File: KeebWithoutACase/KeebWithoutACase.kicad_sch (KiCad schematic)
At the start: 104 parts, among them SW1 SW_Push_45deg, SW10 SW_Push_45deg, SW11 SW_Push_45deg, SW12 SW_Push_45deg, SW13 SW_Push_45deg, SW14 SW_Push_45deg, SW15 SW_Push_45deg, SW16 SW_Push_45deg, SW17 SW_Push_45deg, SW18 SW_Push_45deg, SW19 SW_Push_45deg, SW2 SW_Push_45deg, SW20 SW_Push_45deg, SW21 SW_Push_45deg, SW22 SW_Push_45deg, SW23 SW_Push_45deg, SW24 SW_Push_45deg, SW25 SW_Push_45deg, SW26 SW_Push_45deg, SW27 SW_Push_45deg, SW28 SW_Push_45deg, SW29 SW_Push_45deg, SW3 SW_Push_45deg, SW30 SW_Push_45deg, SW31 SW_Push_45deg, SW32 SW_Push_45deg, SW33 SW_Push_45deg, SW34 SW_Push_45deg, SW35 SW_Push_45deg, SW36 SW_Push_45deg, SW37 SW_Push_45deg, SW38 SW_Push_45deg, SW39 SW_Push_45deg, SW4 SW_Push_45deg, SW40 SW_Push_45deg, SW41 SW_Push_45deg, SW42 SW_Push_45deg, SW43 SW_Push_45deg, SW44 SW_Push_45deg, SW45 SW_Push_45deg, SW46 SW_Push_45deg, SW47 SW_Push_45deg, SW48 SW_Push_45deg, SW49 SW_Push_45deg, SW5 SW_Push_45deg, SW50 SW_Push_45deg, SW51 SW_Push_45deg, SW52 SW_Push_45deg, SW6 SW_Push_45deg, SW7 SW_Push_45deg, SW8 SW_Push_45deg, SW9 SW_Push_45deg

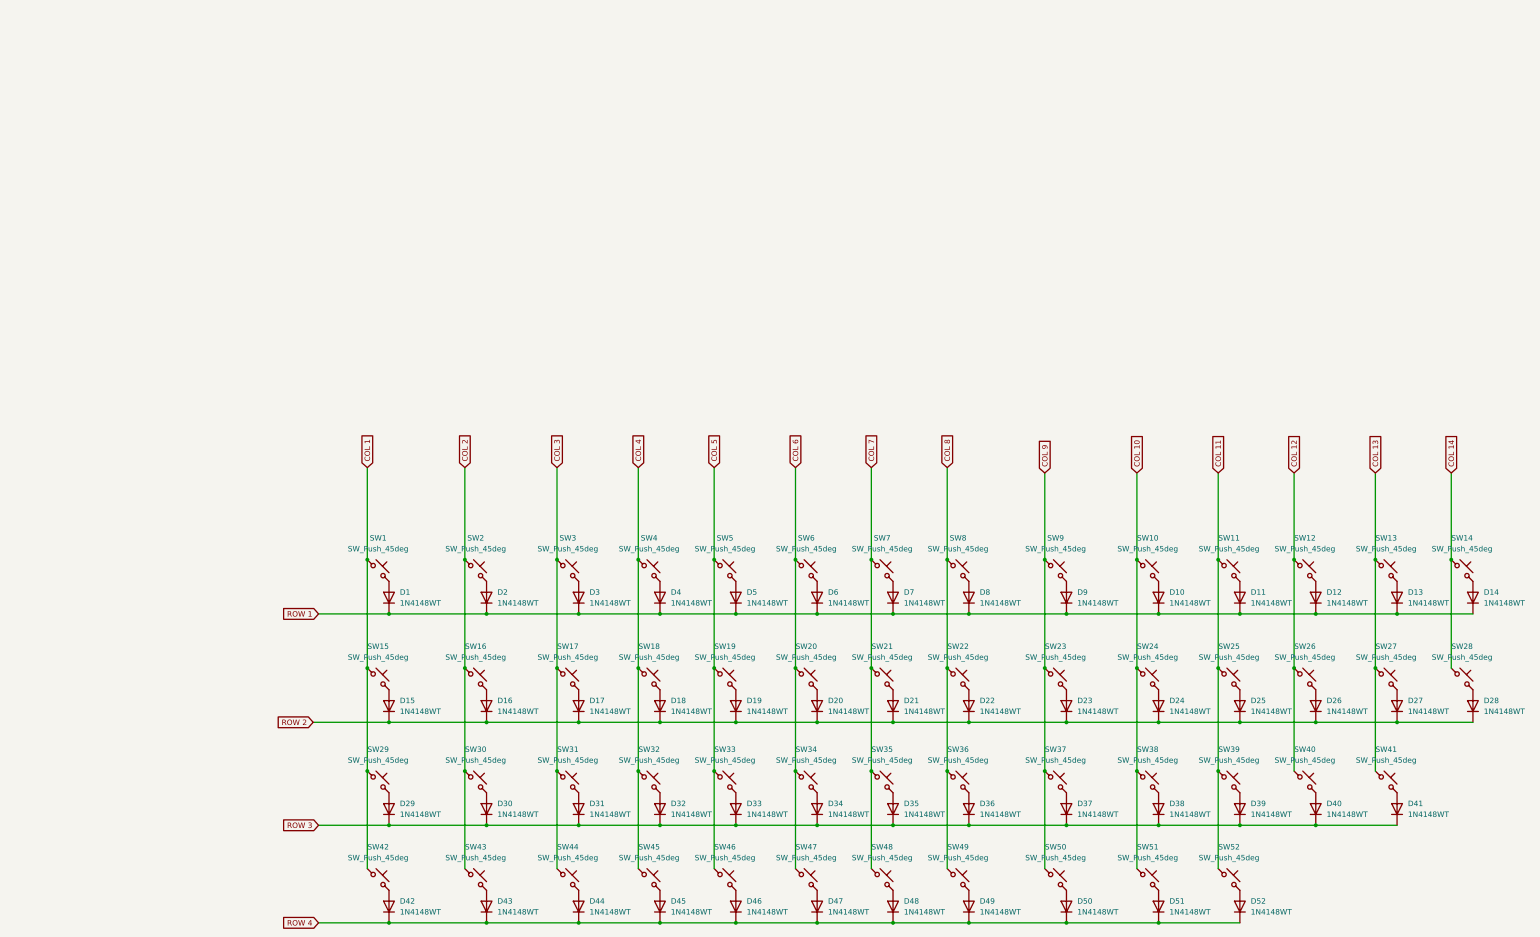
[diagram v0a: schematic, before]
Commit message: updated the schematic of the pcb to include the missing row
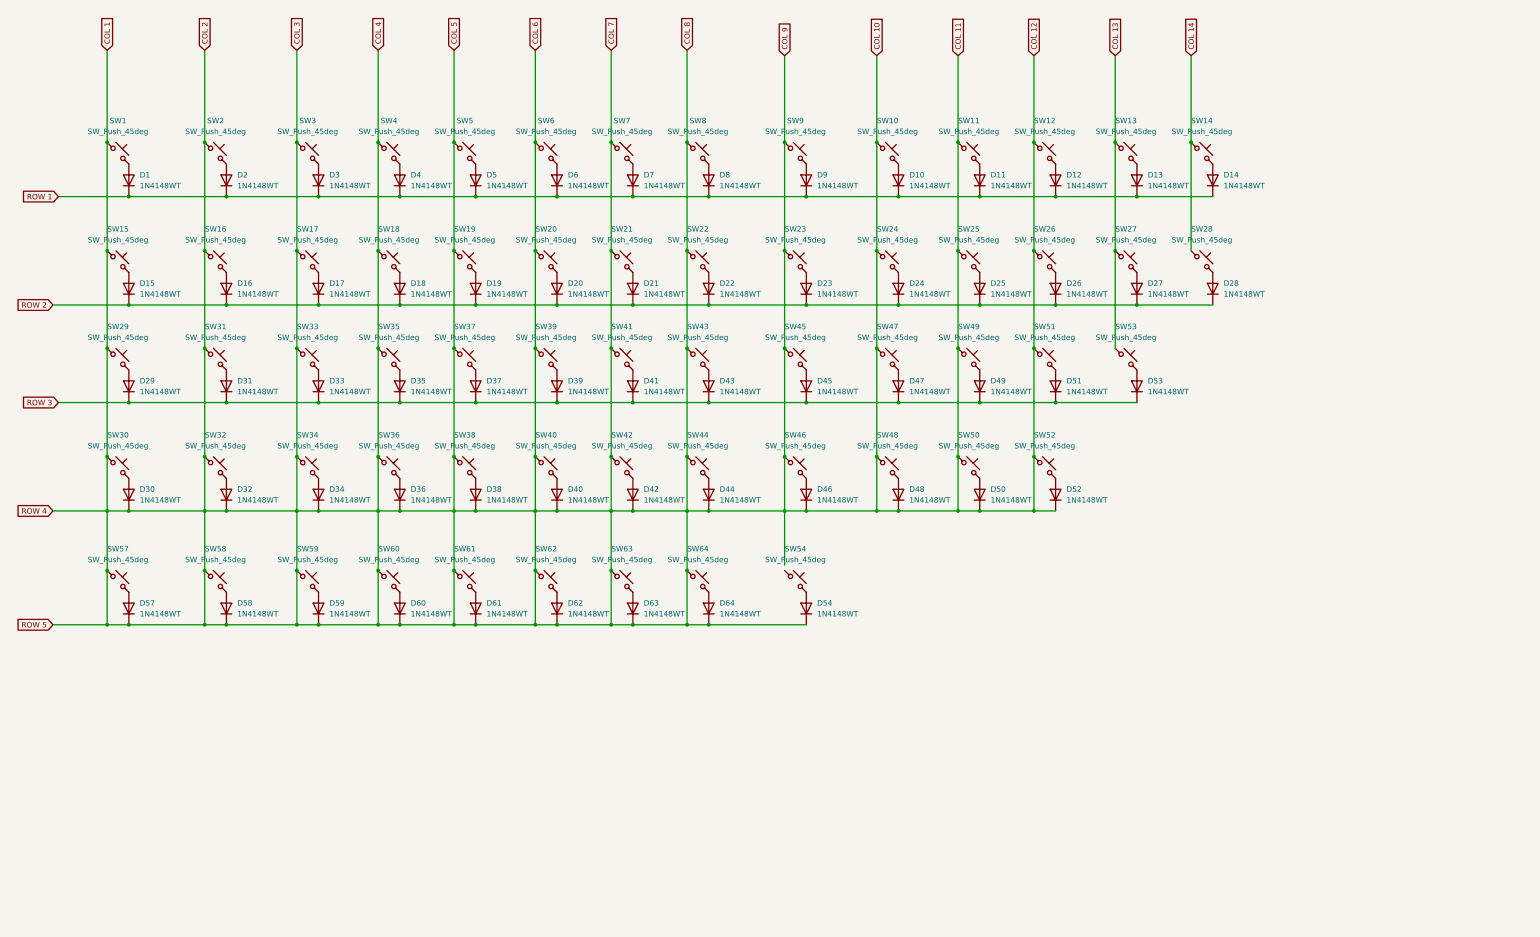
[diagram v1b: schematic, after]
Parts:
- added D53, D54, D57, D58, D59, D60, D61, D62, D63, D64: 1N4148WT, Diode_SMD:D_SOD-523, symbol Diode:1N4148WT
- added SW53, SW54, SW57, SW58, SW59, SW60, SW61, SW62, SW63, SW64: SW_Push_45deg, symbol Switch:SW_Push_45deg
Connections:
- net COL 10 is gone; now on net COL 1: SW10.1, SW24.1, SW38.1, SW51.1
- net COL 11 is gone; now on net COL 1: SW11.1, SW25.1, SW39.1, SW52.1
- net COL 12 is gone; now on net COL 1: SW12.1, SW26.1, SW40.1
- net COL 2 is gone; now on net COL 1: SW16.1, SW2.1, SW30.1, SW43.1
- net COL 3 is gone; now on net COL 1: SW17.1, SW3.1, SW31.1, SW44.1
- net COL 4 is gone; now on net COL 1: SW18.1, SW32.1, SW4.1, SW45.1
- net COL 5 is gone; now on net COL 1: SW19.1, SW33.1, SW46.1, SW5.1
- net COL 6 is gone; now on net COL 1: SW20.1, SW34.1, SW47.1, SW6.1
- net COL 7 is gone; now on net COL 1: SW21.1, SW35.1, SW48.1, SW7.1
- net COL 8 is gone; now on net COL 1: SW22.1, SW36.1, SW49.1, SW8.1
- net COL 9 is gone; now on net COL 1: SW23.1, SW37.1, SW50.1, SW9.1
- net COL 1: now also D30.1 (K), D32.1 (K), D34.1 (K), D36.1 (K), D38.1 (K), D40.1 (K), D42.1 (K), D44.1 (K), D46.1 (K), D48.1 (K), D50.1 (K), D52.1 (K), SW41.1, D54.1 (K), D57.1 (K), D58.1 (K), D59.1 (K), D60.1 (K), D61.1 (K), D62.1 (K), D63.1 (K), D64.1 (K), SW57.1, SW58.1, SW59.1, SW60.1, SW61.1, SW62.1, SW63.1, SW64.1
- net COL 13: now also SW53.1; no longer SW41.1
- net ROW 3: now also D43.1 (K), D45.1 (K), D47.1 (K), D49.1 (K), D51.1 (K), D53.1 (K); no longer D30.1 (K), D32.1 (K), D34.1 (K), D36.1 (K), D38.1 (K), D40.1 (K)
- removed net ROW 4: D42.1 (K), D43.1 (K), D44.1 (K), D45.1 (K), D46.1 (K), D47.1 (K), D48.1 (K), D49.1 (K), D50.1 (K), D51.1 (K), D52.1 (K)
- new net: D53.2 (A), SW53.2
- new net: D60.2 (A), SW60.2
- new net: D57.2 (A), SW57.2
- new net: D62.2 (A), SW62.2
- new net: D54.2 (A), SW54.2
- new net: D63.2 (A), SW63.2
- new net: D64.2 (A), SW64.2
- new net: D58.2 (A), SW58.2
- new net: D61.2 (A), SW61.2
- new net: D59.2 (A), SW59.2
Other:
- moved on the sheet: D1, D10, D11, D12, D13, D14, D15, D16, D17, D18, D19, D2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

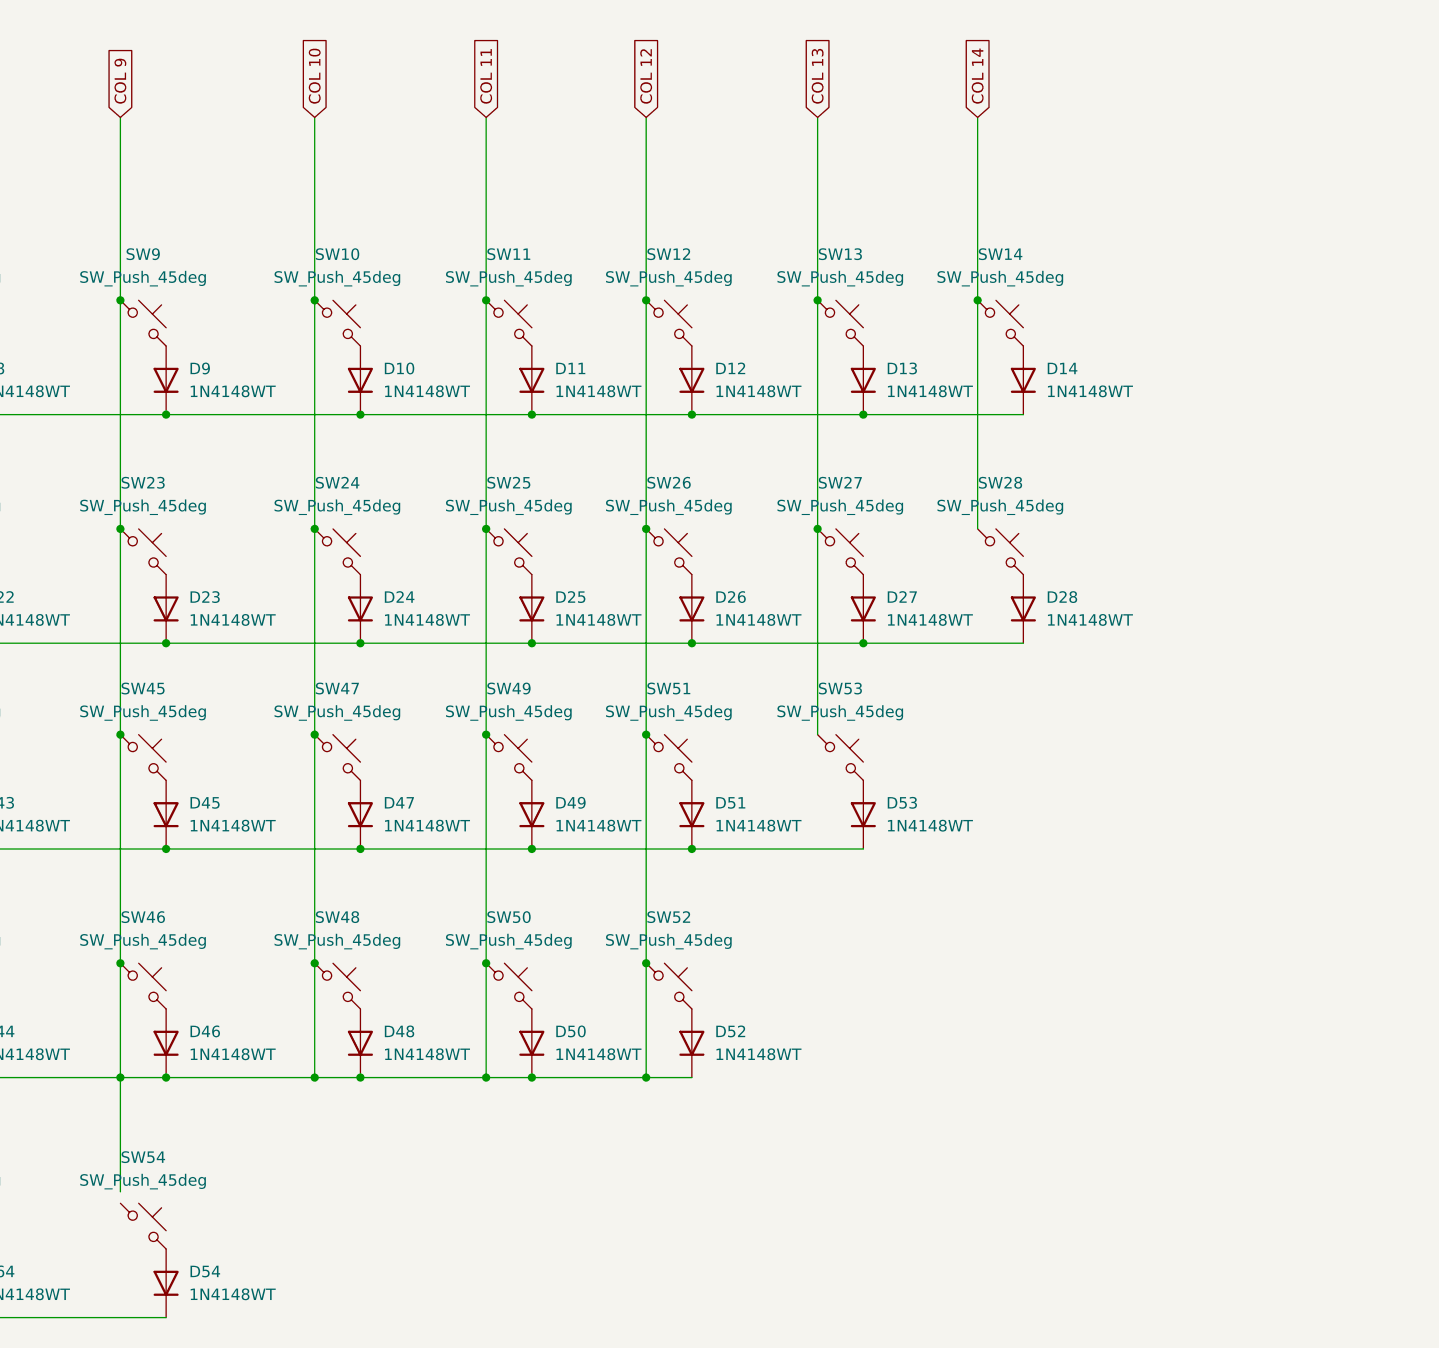
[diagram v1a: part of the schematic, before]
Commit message: updated the schem to incorporate those extra 4 keys
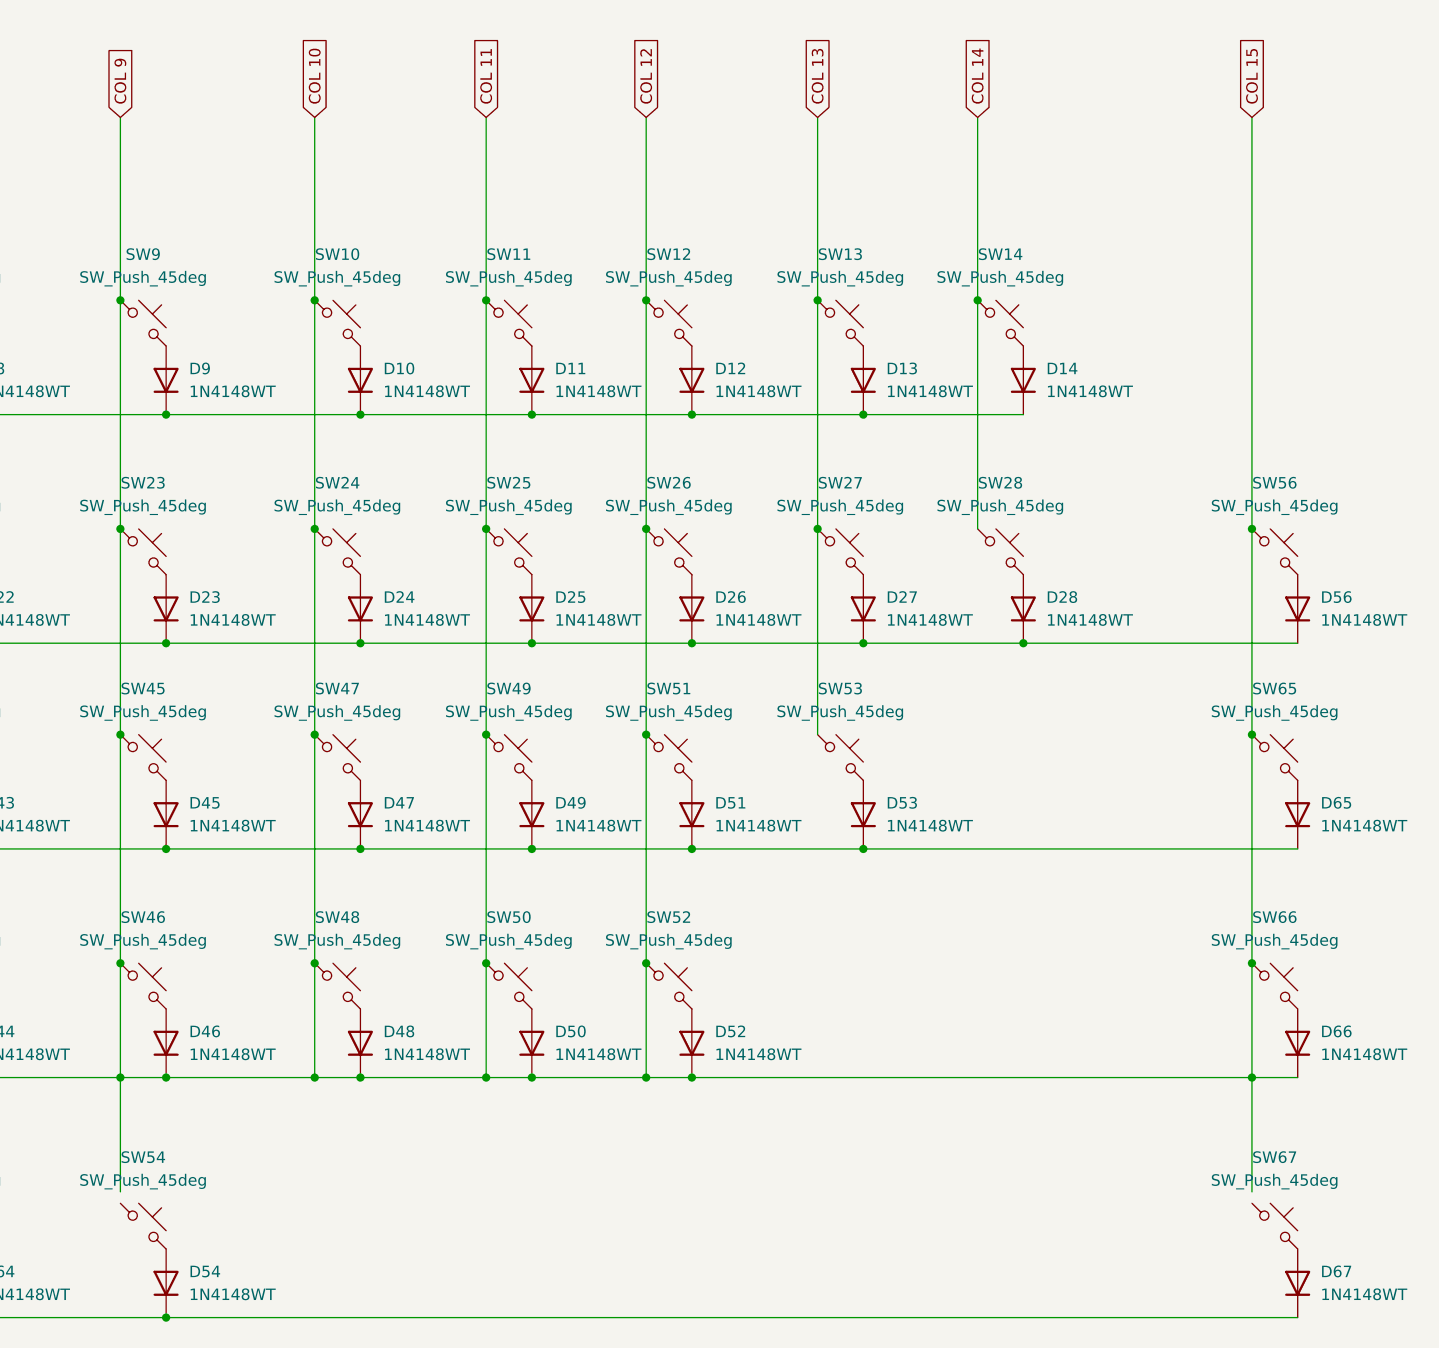
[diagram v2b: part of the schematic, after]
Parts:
- added D56, D65, D66, D67: 1N4148WT, Diode_SMD:D_SOD-523, symbol Diode:1N4148WT
- added SW56, SW65, SW66, SW67: SW_Push_45deg, symbol Switch:SW_Push_45deg
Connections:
- net COL 1: now also D66.1 (K), D67.1 (K), SW56.1, SW65.1, SW66.1
- net ROW 2: now also D56.1 (K)
- net ROW 3: now also D65.1 (K)
- new net: D66.2 (A), SW66.2
- new net: D56.2 (A), SW56.2
- new net: D65.2 (A), SW65.2
- new net: D67.2 (A), SW67.2

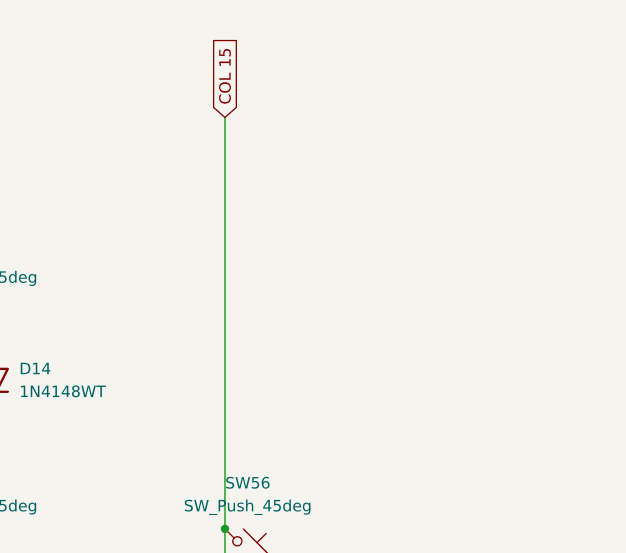
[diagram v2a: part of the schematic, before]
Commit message: added a potentiometer for the volume
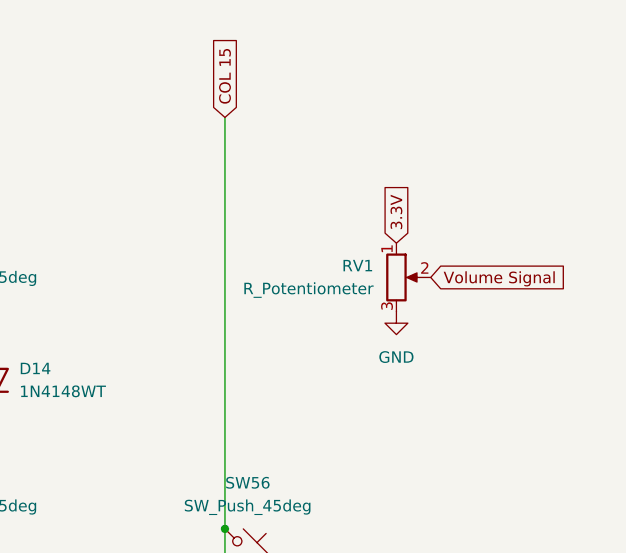
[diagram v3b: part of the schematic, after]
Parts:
- added RV1: R_Potentiometer, symbol Device:R_Potentiometer
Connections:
- new net 3.3V: RV1.1
- new net GND: RV1.3
- new net Volume Signal: RV1.2
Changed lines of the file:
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@@
 		)
 	)
+	(global_label "3.3V"
+		(shape input)
+		(at 374.65 54.61 90)
+		(fields_autoplaced yes)
+		(effects
+			(font
+				(size 1.27 1.27)
+			)
+			(justify left)
+		)
+		(property "Intersheetrefs" "${INTERSHEET_REFS}"
+			(at 374.65 47.5124 90)
+			(effects
+				(font
+					(size 1.27 1.27)
+				)
+				(justify left)
+				(hide yes)
+			)
+		)
+	)
 	(global_label "COL 2"
 		(shape input)
@@
 		)
 	)
+	(global_label "Volume Signal"
+		(shape input)
+		(at 378.46 58.42 0)
+		(fields_autoplaced yes)
+		(effects
+			(font
+				(size 1.27 1.27)
+			)
+			(justify left)
+		)
+		(property "Intersheetrefs" "${INTERSHEET_REFS}"
+			(at 395.173 58.42 0)
+			(effects
+				(font
+					(size 1.27 1.27)
+				)
+				(justify left)
+				(hide yes)
+			)
+		)
+	)
 	(global_label "ROW 1"
 		(shape input)
@@
 	)
 	(symbol
+		(lib_id "Device:R_Potentiometer")
+		(at 374.65 58.42 0)
+		(unit 1)
+		(exclude_from_sim no)
+		(in_bom yes)
+		(on_board yes)
+		(dnp no)
+		(fields_autoplaced yes)
+		(property "Reference" "RV1"
+			(at 372.11 57.1499 0)
+			(effects
+				(font
+					(size 1.27 1.27)
+				)
+				(justify right)
+			)
+		)
+		(property "Value" "R_Potentiometer"
+			(at 372.11 59.6899 0)
+			(effects
+				(font
+					(size 1.27 1.27)
+				)
+				(justify right)
+			)
+		)
+		(property "Footprint" ""
+			(at 374.65 58.42 0)
+			(effects
+				(font
+					(size 1.27 1.27)
+				)
+				(hide yes)
+			)
+		)
+		(property "Datasheet" "~"
+			(at 374.65 58.42 0)
+			(effects
+				(font
+					(size 1.27 1.27)
+				)
+				(hide yes)
+			)
+		)
+		(property "Description" "Potentiometer"
+			(at 374.65 58.42 0)
+			(effects
+				(font
+					(size 1.27 1.27)
+				)
+				(hide yes)
+			)
+		)
+		(pin "3"
+		)
+		(pin "1"
+		)
+		(pin "2"
+		)
+		(instances
+			(project ""
+				(path "/35878fee-9f0f-4654-b50b-b205a4b1f30d"
+					(reference "RV1")
+					(unit 1)
+				)
+			)
+		)
+	)
+	(symbol
 		(lib_id "Switch:SW_Push_45deg")
 		(at 96.52 111.76 0)
@@
 					(unit 1)
 				)
+			)
+		)
+	)
+	(symbol
+		(lib_id "power:GND")
+		(at 374.65 62.23 0)
+		(unit 1)
+		(exclude_from_sim no)
+		(in_bom yes)
+		(on_board yes)
+		(dnp no)
+		(fields_autoplaced yes)
+		(property "Reference" "#PWR01"
+			(at 374.65 68.58 0)
+			(effects
+				(font
+					(size 1.27 1.27)
+				)
+				(hide yes)
+			)
+		)
+		(property "Value" "GND"
+			(at 374.65 67.31 0)
+			(effects
+				(font
+					(size 1.27 1.27)
+				)
+			)
+		)
+		(property "Footprint" ""
+			(at 374.65 62.23 0)
+			(effects
+				(font
+					(size 1.27 1.27)
+				)
+				(hide yes)
+			)
+		)
+		(property "Datasheet" ""
+			(at 374.65 62.23 0)
+			(effects
+				(font
+					(size 1.27 1.27)
+				)
+				(hide yes)
+			)
+		)
+		(property "Description" "Power symbol creates a global label with name \"GND\" , ground"
+			(at 374.65 62.23 0)
+			(effects
+				(font
+					(size 1.27 1.27)
+				)
+				(hide yes)
+			)
+		)
+		(pin "1"
+		)
+		(instances
+			(project ""
+				(path "/35878fee-9f0f-4654-b50b-b205a4b1f30d"
+					(reference "#PWR01")
+					(unit 1)
+				)
